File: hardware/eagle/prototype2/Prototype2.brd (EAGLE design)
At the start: 53 x 59.7 mm, 18 parts, among them U1 ARDUINO_SHIELDLABEL

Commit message: prototype2: resistor values, partlist
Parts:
- R1: value (none) -> 5.6k
- R2: value (none) -> 2.2k
- R3: value (none) -> 50k
- R4: value (none) -> 22k
- R5: value (none) -> 10k
- R6: value (none) -> 100k
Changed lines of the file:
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@@
 <element name="U1" library="SparkFun" package="DUEMILANOVE_SHIELD" value="ARDUINO_SHIELDLABEL" x="0" y="0"/>
 <element name="U$3" library="CAT4016" package="SOIC24W" value="CAT4016" x="26.035" y="40.005" rot="R270"/>
-<element name="R2" library="rcl" package="0204/7" value="" x="27.305" y="50.165"/>
-<element name="R5" library="rcl" package="RTRIM3165W" value="" x="20.955" y="51.435"/>
+<element name="R2" library="rcl" package="0204/7" value="2.2k" x="27.305" y="50.165"/>
+<element name="R5" library="rcl" package="RTRIM3165W" value="10k" x="20.955" y="51.435"/>
 <element name="C1" library="rcl" package="A/3216-18W" value="" x="35.56" y="44.45" rot="MR90"/>
 <element name="U$1" library="CAT4016" package="SOIC24W" value="CAT4016" x="26.035" y="22.86" rot="R90"/>
-<element name="R1" library="rcl" package="0204/7" value="" x="27.94" y="10.795" rot="MR180"/>
-<element name="R3" library="rcl" package="RTRIM3165W" value="" x="36.83" y="11.43" rot="R270"/>
+<element name="R1" library="rcl" package="0204/7" value="5.6k" x="27.94" y="10.795" rot="MR180"/>
+<element name="R3" library="rcl" package="RTRIM3165W" value="50k" x="36.83" y="11.43" rot="R270"/>
 <element name="C2" library="rcl" package="A/3216-18W" value="" x="13.97" y="15.875"/>
 <element name="U$2" library="CAT4016" package="SOIC24W" value="CAT4016" x="26.035" y="23.495" rot="MR90"/>
-<element name="R4" library="rcl" package="0204/7" value="" x="27.94" y="13.335" rot="MR0"/>
-<element name="R6" library="rcl" package="RTRIM3165W" value="" x="36.83" y="15.875" rot="R270"/>
+<element name="R4" library="rcl" package="0204/7" value="22k" x="27.94" y="13.335" rot="MR0"/>
+<element name="R6" library="rcl" package="RTRIM3165W" value="100k" x="36.83" y="15.875" rot="R270"/>
 <element name="C3" library="rcl" package="A/3216-18W" value="" x="41.275" y="18.415" rot="MR180"/>
 <element name="LED1" library="customized" package="P-LCC-6_TOPLED" value="MULTILED_LRTB_G6TG" x="41.275" y="51.435" rot="R90"/>

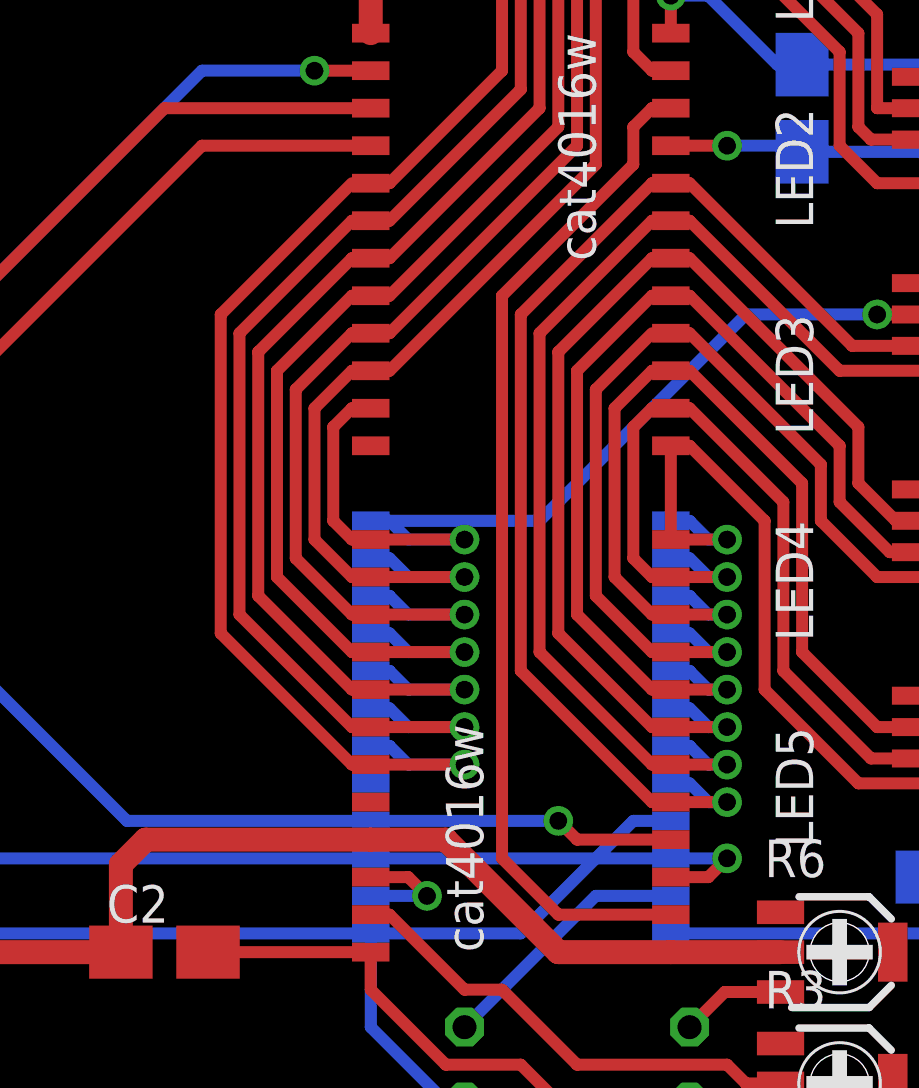
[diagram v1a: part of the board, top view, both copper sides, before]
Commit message: Prototype2: Layout-update. doc: parts-list prototype 2
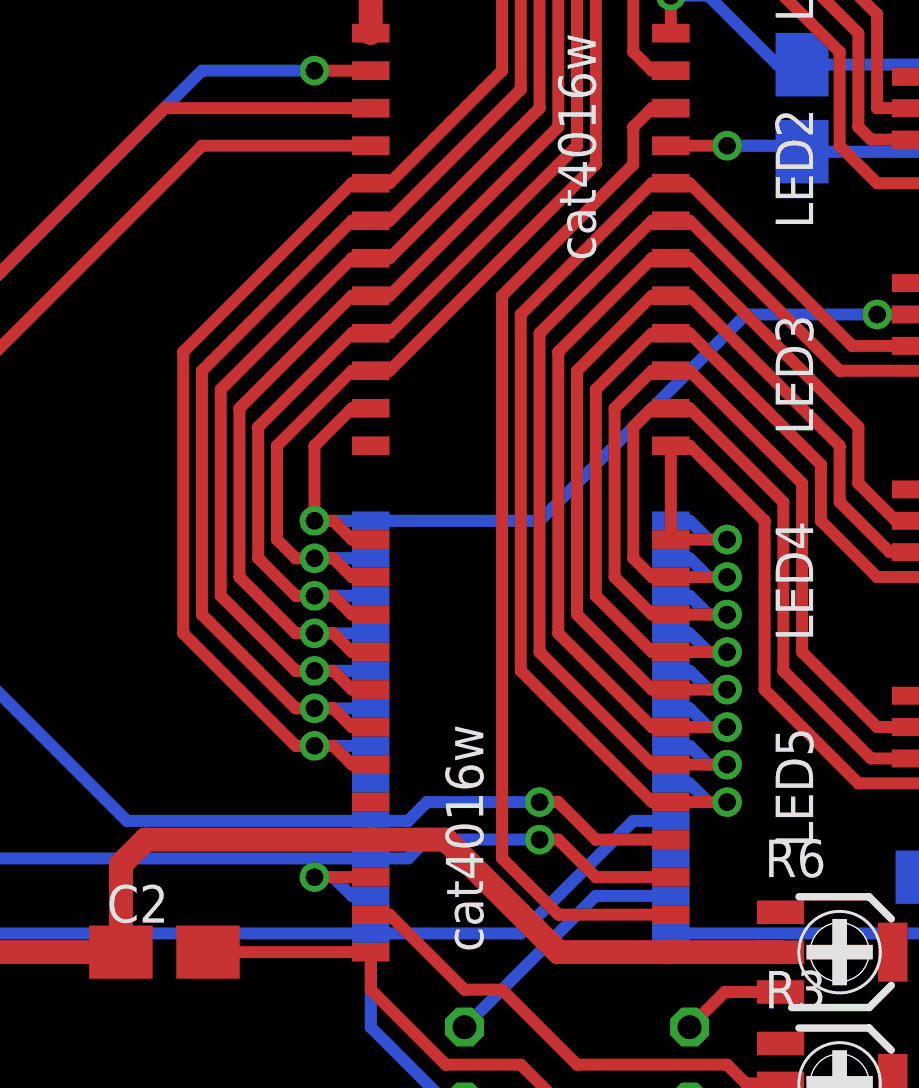
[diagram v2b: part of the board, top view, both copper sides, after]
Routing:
- net N$25: track 34.0 -> 30.2 mm
- net N$14: track 73.2 -> 69.9 mm, vias 0 -> 1
- net N$39: track 57.8 -> 54.9 mm
- net N$32: track 53.1 -> 50.2 mm
- net N$31: track 55.9 -> 53.0 mm
- net N$34: track 59.8 -> 56.9 mm
- net N$33: track 55.3 -> 52.3 mm
- net N$43: track 59.5 -> 57.3 mm
- net N$6: track 56.7 -> 57.2 mm, vias 0 -> 1

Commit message: Gerber files for updated Prototype2
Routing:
- net GND: track 176.6 -> 176.0 mm
- net +5V: track 181.9 -> 181.3 mm
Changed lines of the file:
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@@
 <wire x1="53.01" y1="59.68" x2="0" y2="59.68" width="0" layer="20"/>
 <wire x1="0" y1="59.68" x2="0" y2="0" width="0" layer="20"/>
-<text x="52.07" y="1.27" size="1.778" layer="16" rot="MR0">BOT</text>
-<text x="46.99" y="1.27" size="1.778" layer="1">TOP</text>
 <text x="7.62" y="3.175" size="1.4224" layer="1" ratio="20">TOP</text>
 <text x="17.145" y="3.175" size="1.4224" layer="16" ratio="20" rot="MR0">BOT</text>
@@
 <contactref element="U1" pad="GND@1"/>
 <contactref element="U1" pad="GND@2"/>
-<polygon width="0.4064" layer="16">
+<polygon width="0.4064" layer="16" orphans="yes">
 <vertex x="0" y="59.69"/>
 <vertex x="53.34" y="59.69"/>
@@
 <wire x1="31.115" y1="20.32" x2="29.845" y2="20.32" width="0.4064" layer="16"/>
 <wire x1="29.845" y1="20.32" x2="26.035" y2="16.51" width="0.4064" layer="16"/>
-<wire x1="4.24" y1="16.08" x2="3.81" y2="16.51" width="0.4064" layer="16"/>
 <wire x1="3.81" y1="16.51" x2="2.54" y2="17.78" width="0.4064" layer="16"/>
 <wire x1="12.495" y1="15.875" x2="4.445" y2="15.875" width="0.8128" layer="1"/>
@@
 <wire x1="20.955" y1="50.165" x2="26.67" y2="55.88" width="0.8128" layer="1"/>
 <wire x1="26.67" y1="55.88" x2="43.18" y2="55.88" width="0.8128" layer="1"/>
-<wire x1="43.18" y1="55.88" x2="46.99" y2="52.07" width="0.8128" layer="1"/>
-<wire x1="46.99" y1="52.07" x2="46.99" y2="35.56" width="0.8128" layer="1"/>
-<wire x1="46.99" y1="35.56" x2="50.8" y2="31.75" width="0.8128" layer="1"/>
+<wire x1="43.18" y1="55.88" x2="46.355" y2="52.705" width="0.8128" layer="1"/>
+<wire x1="46.355" y1="52.705" x2="46.355" y2="36.195" width="0.8128" layer="1"/>
+<wire x1="46.355" y1="36.195" x2="50.8" y2="31.75" width="0.8128" layer="1"/>
 <wire x1="50.8" y1="34.29" x2="50.8" y2="31.75" width="0.4064" layer="1"/>
 <wire x1="31.115" y1="43.18" x2="33.02" y2="43.18" width="0.4064" layer="1"/>
@@
 <wire x1="20.955" y1="14.605" x2="23.495" y2="12.065" width="0.4064" layer="1"/>
 <wire x1="23.495" y1="12.065" x2="26.035" y2="12.065" width="0.4064" layer="1"/>
-<wire x1="26.035" y1="12.065" x2="29.845" y2="8.255" width="0.4064" layer="1"/>
-<wire x1="29.845" y1="8.255" x2="38.1" y2="8.255" width="0.4064" layer="1"/>
-<wire x1="38.1" y1="8.255" x2="44.45" y2="14.605" width="0.4064" layer="1"/>
+<wire x1="26.035" y1="12.065" x2="29.21" y2="8.89" width="0.4064" layer="1"/>
+<wire x1="29.21" y1="8.89" x2="38.735" y2="8.89" width="0.4064" layer="1"/>
+<wire x1="38.735" y1="8.89" x2="44.45" y2="14.605" width="0.4064" layer="1"/>
 <wire x1="20.955" y1="15.875" x2="15.445" y2="15.875" width="0.4064" layer="1"/>
 <wire x1="42.75" y1="18.415" x2="42.75" y2="16.715" width="0.4064" layer="16"/>
@@
 <wire x1="19.685" y1="30.48" x2="20.32" y2="29.845" width="0.4064" layer="1"/>
 <wire x1="20.32" y1="29.845" x2="20.955" y2="29.845" width="0.4064" layer="1"/>
+<wire x1="20.955" y1="30.48" x2="19.05" y2="30.48" width="0.4064" layer="16"/>
 <wire x1="38.1" y1="37.465" x2="38.1" y2="37.465" width="0" layer="19" extent="1-16"/>
-<wire x1="20.955" y1="30.48" x2="19.05" y2="30.48" width="0.4064" layer="16"/>
 <wire x1="19.05" y1="30.48" x2="19.05" y2="30.48" width="0" layer="19" extent="1-16"/>
 </signal>
@@
 <wire x1="20.32" y1="28.575" x2="20.955" y2="28.575" width="0.4064" layer="1"/>
 <wire x1="20.955" y1="29.21" x2="19.05" y2="29.21" width="0.4064" layer="16"/>
-<wire x1="19.05" y1="29.21" x2="19.05" y2="29.21" width="0" layer="19" extent="1-16"/>
+<wire x1="20.955" y1="29.21" x2="20.955" y2="28.575" width="0" layer="19" extent="1-16"/>
 </signal>
 <signal name="N$32">
@@
 <wire x1="20.32" y1="27.305" x2="20.955" y2="27.305" width="0.4064" layer="1"/>
 <wire x1="20.955" y1="27.94" x2="19.05" y2="27.94" width="0.4064" layer="16"/>
-<wire x1="19.05" y1="27.94" x2="19.05" y2="27.94" width="0" layer="19" extent="1-16"/>
+<wire x1="20.955" y1="27.305" x2="20.955" y2="27.94" width="0" layer="19" extent="1-16"/>
 </signal>
 <signal name="N$33">
@@
 <wire x1="18.415" y1="26.67" x2="19.685" y2="26.67" width="0.4064" layer="1"/>
 <wire x1="19.685" y1="26.67" x2="20.32" y2="26.035" width="0.4064" layer="1"/>
+<wire x1="20.955" y1="26.67" x2="19.05" y2="26.67" width="0.4064" layer="16"/>
 <wire x1="38.735" y1="44.45" x2="39.21" y2="44.45" width="0" layer="19" extent="1-1"/>
-<wire x1="20.955" y1="26.67" x2="19.05" y2="26.67" width="0.4064" layer="16"/>
-<wire x1="19.05" y1="26.67" x2="19.05" y2="26.67" width="0" layer="19" extent="1-16"/>
+<wire x1="20.955" y1="26.67" x2="20.955" y2="26.035" width="0" layer="19" extent="1-16"/>
 </signal>
 <signal name="N$34">
@@
 <wire x1="19.685" y1="25.4" x2="20.32" y2="24.765" width="0.4064" layer="1"/>
 <wire x1="20.955" y1="25.4" x2="19.05" y2="25.4" width="0.4064" layer="16"/>
-<wire x1="19.05" y1="25.4" x2="19.05" y2="25.4" width="0" layer="19" extent="1-16"/>
+<wire x1="20.955" y1="25.4" x2="20.955" y2="24.765" width="0" layer="19" extent="1-16"/>
 </signal>
 <signal name="N$39">
@@
 <wire x1="18.415" y1="24.13" x2="19.685" y2="24.13" width="0.4064" layer="1"/>
 <wire x1="19.685" y1="24.13" x2="20.32" y2="23.495" width="0.4064" layer="1"/>
+<wire x1="20.955" y1="24.13" x2="19.05" y2="24.13" width="0.4064" layer="16"/>
 <wire x1="39.37" y1="50.165" x2="39.21" y2="50.3725" width="0" layer="19" extent="1-1"/>
-<wire x1="20.955" y1="24.13" x2="19.05" y2="24.13" width="0.4064" layer="16"/>
-<wire x1="19.05" y1="24.13" x2="19.05" y2="24.13" width="0" layer="19" extent="1-16"/>
+<wire x1="20.955" y1="24.13" x2="20.955" y2="23.495" width="0" layer="19" extent="1-16"/>
 </signal>
 <signal name="N$43">
@@
 <wire x1="20.32" y1="22.225" x2="20.955" y2="22.225" width="0.4064" layer="1"/>
 <wire x1="20.955" y1="22.86" x2="19.05" y2="22.86" width="0.4064" layer="16"/>
-<wire x1="19.05" y1="22.86" x2="19.05" y2="22.86" width="0" layer="19" extent="1-16"/>
+<wire x1="20.955" y1="22.225" x2="20.955" y2="22.86" width="0" layer="19" extent="1-16"/>
 </signal>
 <signal name="N$51">

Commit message: temporary Colorpicker
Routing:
- net GND: track 176.0 -> 183.4 mm
- net +5V: track 181.3 -> 183.4 mm
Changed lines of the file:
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@@
 <wire x1="20.955" y1="16.51" x2="3.81" y2="16.51" width="0.4064" layer="16"/>
 <wire x1="20.955" y1="49.435" x2="20.955" y2="50.165" width="0.4064" layer="1"/>
-<wire x1="20.955" y1="50.165" x2="26.67" y2="55.88" width="0.8128" layer="1"/>
 <wire x1="26.67" y1="55.88" x2="43.18" y2="55.88" width="0.8128" layer="1"/>
 <wire x1="43.18" y1="55.88" x2="46.355" y2="52.705" width="0.8128" layer="1"/>
@@
 <wire x1="39.575" y1="42.975" x2="50.8" y2="31.75" width="0.4064" layer="16"/>
 <wire x1="33.02" y1="43.18" x2="33.02" y2="43.18" width="0" layer="19" extent="1-16"/>
+<wire x1="26.67" y1="55.88" x2="24.765" y2="53.975" width="0.8128" layer="1"/>
+<wire x1="24.765" y1="53.975" x2="24.765" y2="48.895" width="0.8128" layer="1"/>
+<wire x1="24.765" y1="48.895" x2="22.86" y2="46.99" width="0.8128" layer="1"/>
+<wire x1="22.86" y1="46.99" x2="20.955" y2="46.99" width="0.8128" layer="1"/>
+<wire x1="20.955" y1="46.99" x2="20.955" y2="50.165" width="0.8128" layer="1"/>
 </signal>
 <signal name="+5V">
@@
 <wire x1="44.0225" y1="24.5575" x2="44.45" y2="24.13" width="0.4064" layer="1"/>
 <wire x1="44.45" y1="24.13" x2="44.45" y2="22.86" width="0.4064" layer="1"/>
-<wire x1="31.115" y1="16.51" x2="42.545" y2="16.51" width="0.4064" layer="16"/>
 <wire x1="42.545" y1="16.51" x2="43.815" y2="16.51" width="0.4064" layer="16"/>
 <wire x1="43.815" y1="16.51" x2="48.26" y2="20.955" width="0.4064" layer="16"/>
@@
 <wire x1="52.705" y1="38.735" x2="52.705" y2="31.115" width="0.4064" layer="16"/>
 <wire x1="52.705" y1="31.115" x2="50.8" y2="29.21" width="0.4064" layer="16"/>
+<wire x1="31.115" y1="16.51" x2="33.02" y2="16.51" width="0.4064" layer="16"/>
+<wire x1="33.02" y1="16.51" x2="35.56" y2="13.97" width="0.4064" layer="16"/>
+<wire x1="35.56" y1="13.97" x2="38.1" y2="13.97" width="0.4064" layer="16"/>
+<wire x1="38.1" y1="13.97" x2="40.64" y2="16.51" width="0.4064" layer="16"/>
+<wire x1="40.64" y1="16.51" x2="42.545" y2="16.51" width="0.4064" layer="16"/>
 </signal>
 <signal name="N$26">
@@
 <contactref element="U$1" pad="22"/>
 <contactref element="U$2" pad="2"/>
-<wire x1="20.955" y1="18.415" x2="19.05" y2="18.415" width="0.4064" layer="1"/>
-<wire x1="20.955" y1="17.78" x2="20.32" y2="17.78" width="0.4064" layer="16"/>
-<wire x1="20.32" y1="17.78" x2="19.685" y2="18.415" width="0.4064" layer="16"/>
-<wire x1="19.685" y1="18.415" x2="19.05" y2="18.415" width="0.4064" layer="16"/>
-<wire x1="19.05" y1="18.415" x2="19.05" y2="18.415" width="0" layer="19" extent="1-16"/>
+<wire x1="20.955" y1="17.78" x2="19.05" y2="17.78" width="0.4064" layer="16"/>
+<wire x1="20.955" y1="18.415" x2="20.32" y2="18.415" width="0.4064" layer="1"/>
+<wire x1="20.32" y1="18.415" x2="19.685" y2="17.78" width="0.4064" layer="1"/>
+<wire x1="19.685" y1="17.78" x2="19.05" y2="17.78" width="0.4064" layer="1"/>
+<wire x1="19.05" y1="17.78" x2="19.05" y2="17.78" width="0" layer="19" extent="1-16"/>
 </signal>
 <signal name="N$3">
@@
 <contactref element="LED2" pad="C2"/>
 <wire x1="20.955" y1="35.56" x2="21.59" y2="35.56" width="0.4064" layer="1"/>
-<wire x1="21.59" y1="35.56" x2="28.575" y2="42.545" width="0.4064" layer="1"/>
-<wire x1="28.575" y1="42.545" x2="28.575" y2="49.53" width="0.4064" layer="1"/>
-<wire x1="28.575" y1="49.53" x2="30.48" y2="51.435" width="0.4064" layer="1"/>
+<wire x1="21.59" y1="35.56" x2="29.21" y2="43.18" width="0.4064" layer="1"/>
+<wire x1="29.21" y1="43.18" x2="29.21" y2="50.165" width="0.4064" layer="1"/>
+<wire x1="29.21" y1="50.165" x2="30.48" y2="51.435" width="0.4064" layer="1"/>
 <wire x1="30.48" y1="51.435" x2="31.75" y2="51.435" width="0.4064" layer="1"/>
 <wire x1="31.75" y1="51.435" x2="36.83" y2="46.355" width="0.4064" layer="1"/>
@@
 <contactref element="LED2" pad="C1"/>
 <wire x1="20.955" y1="36.83" x2="21.59" y2="36.83" width="0.4064" layer="1"/>
-<wire x1="21.59" y1="36.83" x2="27.94" y2="43.18" width="0.4064" layer="1"/>
-<wire x1="27.94" y1="43.18" x2="27.94" y2="50.165" width="0.4064" layer="1"/>
-<wire x1="27.94" y1="50.165" x2="29.845" y2="52.07" width="0.4064" layer="1"/>
+<wire x1="21.59" y1="36.83" x2="28.575" y2="43.815" width="0.4064" layer="1"/>
+<wire x1="28.575" y1="43.815" x2="28.575" y2="50.8" width="0.4064" layer="1"/>
+<wire x1="28.575" y1="50.8" x2="29.845" y2="52.07" width="0.4064" layer="1"/>
 <wire x1="29.845" y1="52.07" x2="32.385" y2="52.07" width="0.4064" layer="1"/>
 <wire x1="32.385" y1="52.07" x2="37.465" y2="46.99" width="0.4064" layer="1"/>
@@
 <contactref element="LED2" pad="C3"/>
 <wire x1="20.955" y1="38.1" x2="21.59" y2="38.1" width="0.4064" layer="1"/>
-<wire x1="21.59" y1="38.1" x2="27.305" y2="43.815" width="0.4064" layer="1"/>
-<wire x1="27.305" y1="43.815" x2="27.305" y2="50.8" width="0.4064" layer="1"/>
-<wire x1="27.305" y1="50.8" x2="29.21" y2="52.705" width="0.4064" layer="1"/>
+<wire x1="21.59" y1="38.1" x2="27.94" y2="44.45" width="0.4064" layer="1"/>
+<wire x1="27.94" y1="44.45" x2="27.94" y2="51.435" width="0.4064" layer="1"/>
+<wire x1="27.94" y1="51.435" x2="29.21" y2="52.705" width="0.4064" layer="1"/>
 <wire x1="29.21" y1="52.705" x2="33.02" y2="52.705" width="0.4064" layer="1"/>
 <wire x1="33.02" y1="52.705" x2="38.1" y2="47.625" width="0.4064" layer="1"/>
@@
 <contactref element="LED1" pad="C2"/>
 <wire x1="20.955" y1="39.37" x2="21.59" y2="39.37" width="0.4064" layer="1"/>
-<wire x1="21.59" y1="39.37" x2="26.67" y2="44.45" width="0.4064" layer="1"/>
-<wire x1="26.67" y1="44.45" x2="26.67" y2="51.435" width="0.4064" layer="1"/>
-<wire x1="26.67" y1="51.435" x2="28.575" y2="53.34" width="0.4064" layer="1"/>
+<wire x1="21.59" y1="39.37" x2="27.305" y2="45.085" width="0.4064" layer="1"/>
+<wire x1="27.305" y1="45.085" x2="27.305" y2="52.07" width="0.4064" layer="1"/>
+<wire x1="27.305" y1="52.07" x2="28.575" y2="53.34" width="0.4064" layer="1"/>
 <wire x1="28.575" y1="53.34" x2="34.29" y2="53.34" width="0.4064" layer="1"/>
 <wire x1="34.29" y1="53.34" x2="38.1" y2="49.53" width="0.4064" layer="1"/>
@@
 <contactref element="LED1" pad="C1"/>
 <wire x1="20.955" y1="40.64" x2="21.59" y2="40.64" width="0.4064" layer="1"/>
-<wire x1="21.59" y1="40.64" x2="26.035" y2="45.085" width="0.4064" layer="1"/>
-<wire x1="26.035" y1="45.085" x2="26.035" y2="52.07" width="0.4064" layer="1"/>
-<wire x1="26.035" y1="52.07" x2="27.94" y2="53.975" width="0.4064" layer="1"/>
+<wire x1="21.59" y1="40.64" x2="26.67" y2="45.72" width="0.4064" layer="1"/>
+<wire x1="26.67" y1="45.72" x2="26.67" y2="52.705" width="0.4064" layer="1"/>
+<wire x1="26.67" y1="52.705" x2="27.94" y2="53.975" width="0.4064" layer="1"/>
 <wire x1="27.94" y1="53.975" x2="34.925" y2="53.975" width="0.4064" layer="1"/>
 <wire x1="34.925" y1="53.975" x2="38.735" y2="50.165" width="0.4064" layer="1"/>
@@
 <contactref element="LED1" pad="C3"/>
 <wire x1="20.955" y1="41.91" x2="21.59" y2="41.91" width="0.4064" layer="1"/>
-<wire x1="21.59" y1="41.91" x2="25.4" y2="45.72" width="0.4064" layer="1"/>
-<wire x1="25.4" y1="45.72" x2="25.4" y2="52.705" width="0.4064" layer="1"/>
-<wire x1="25.4" y1="52.705" x2="27.305" y2="54.61" width="0.4064" layer="1"/>
+<wire x1="21.59" y1="41.91" x2="26.035" y2="46.355" width="0.4064" layer="1"/>
+<wire x1="26.035" y1="46.355" x2="26.035" y2="53.34" width="0.4064" layer="1"/>
+<wire x1="26.035" y1="53.34" x2="27.305" y2="54.61" width="0.4064" layer="1"/>
 <wire x1="27.305" y1="54.61" x2="35.56" y2="54.61" width="0.4064" layer="1"/>
 <wire x1="35.56" y1="54.61" x2="38.735" y2="51.435" width="0.4064" layer="1"/>
@@
 </signal>
 <signal name="N$24">
-<via x="19.05" y="18.415" extent="1-16" drill="0.6" shape="square"/>
+<via x="19.05" y="17.78" extent="1-16" drill="0.6" shape="square"/>
 </signal>
 </signals>
